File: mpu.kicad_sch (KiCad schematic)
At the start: 10 parts, among them U501 STM32MP135FAE7

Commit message: Reorganize schema
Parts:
- renumbered C502 to C401, C501 to C402, R502 to R401, R501 to R402, TP501 to TP401, TP502 to TP402, TP503 to TP403, TP504 to TP404, TP505 to TP405, U501 to U401
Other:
- added sheet MPU PMIC (mpu_pmic.kicad_sch)
- moved on the sheet: C401, C402, R401, R402, TP401, TP402, TP403, TP404, TP405, U401C, U401D, U401E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

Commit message: Add MPU boot selection
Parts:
- added R403, R404, R405: 1 kΩ, perfect_footprints:R_0402_1005Metric, symbol Device:R
- added SW401: SW_DIP_x03, symbol Switch:SW_DIP_x03
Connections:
- net GND: now also SW401.4, SW401.5, SW401.6
- net VDD: now also R403.1, R404.1, R405.1
- net RX: now reaches U401.C5 (PD8)
- net TX: now reaches U401.D2 (PD6)
- net BOOT1: now reaches U401.H2 (PI3)
- net BOOT1: now also R404.2, SW401.2
- net BOOT2: now reaches U401.J3 (PI2)
- net BOOT2: now also R403.2, SW401.3
- net BOOT0: now reaches U401.U14 (PI4)
- net BOOT0: now also R405.2, SW401.1
- no-connect marks 128 -> 123
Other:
- moved on the sheet: C401, C402, R401, R402, TP401, TP402, TP403, TP404, TP405, U401C, U401D, U401E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

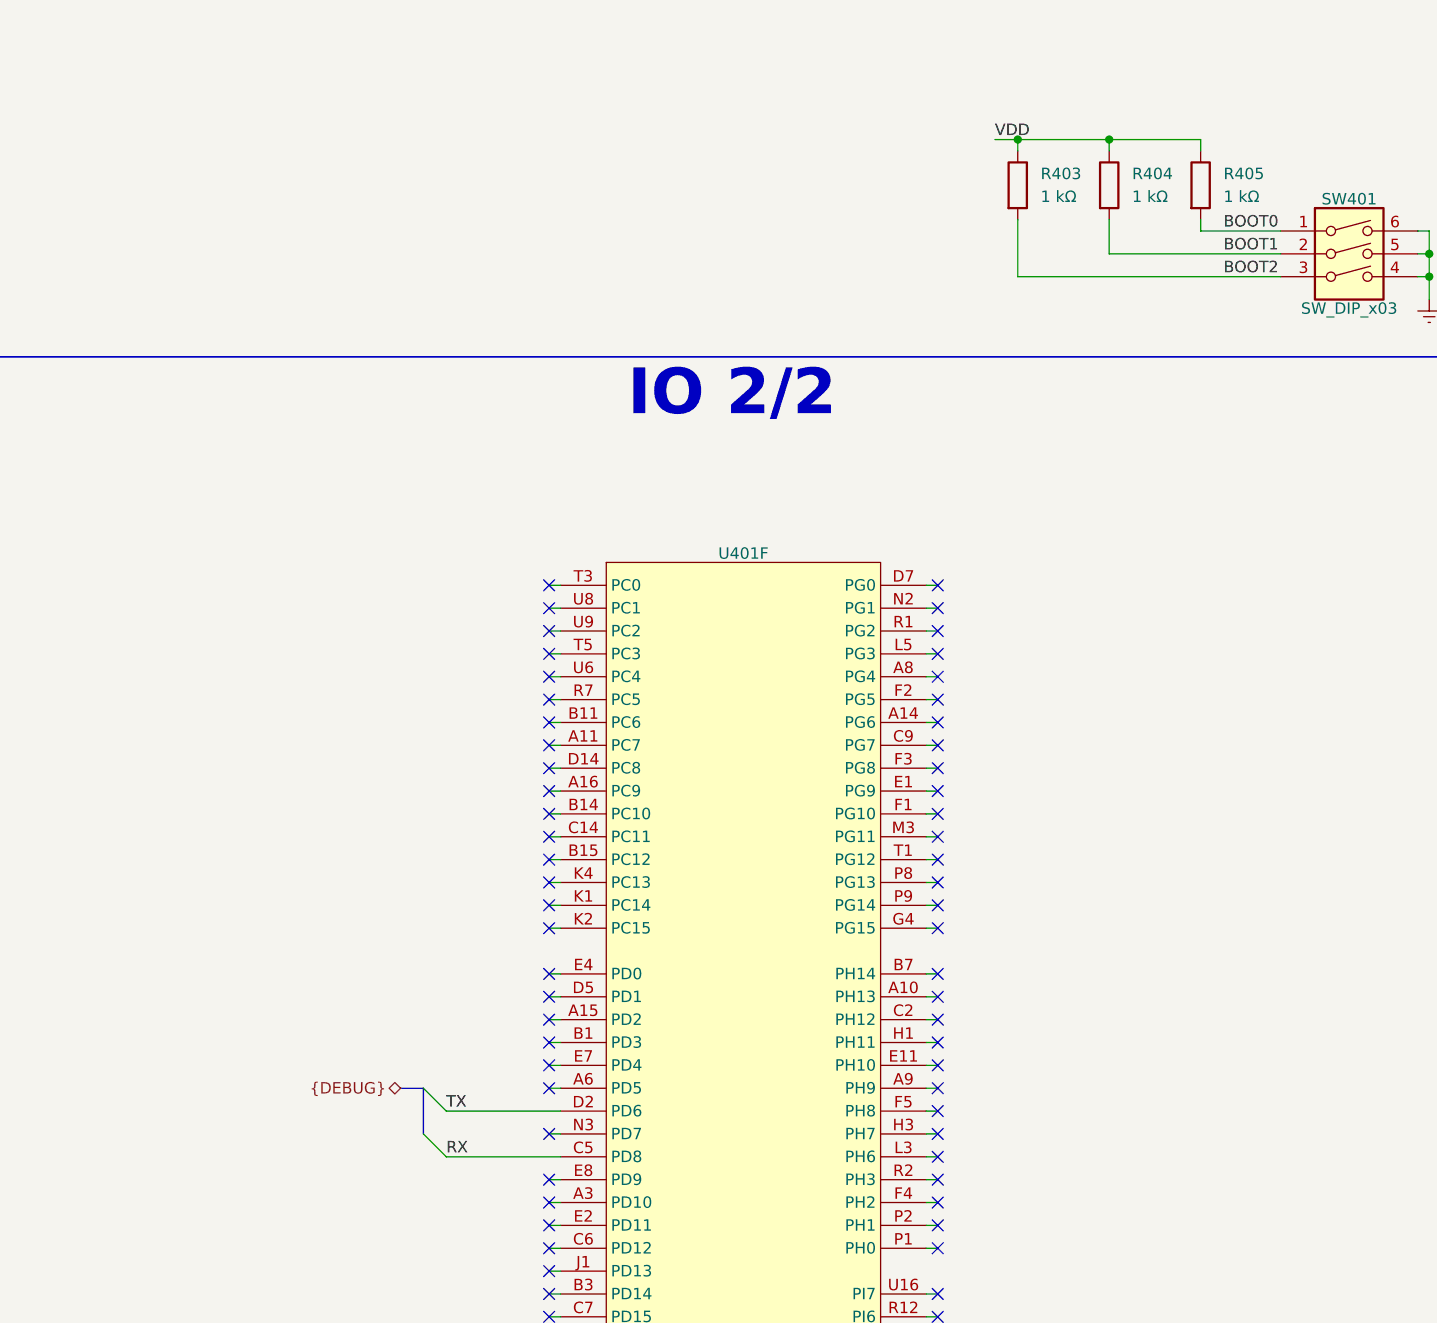
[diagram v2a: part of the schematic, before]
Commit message: Add USB-to-UART debug option
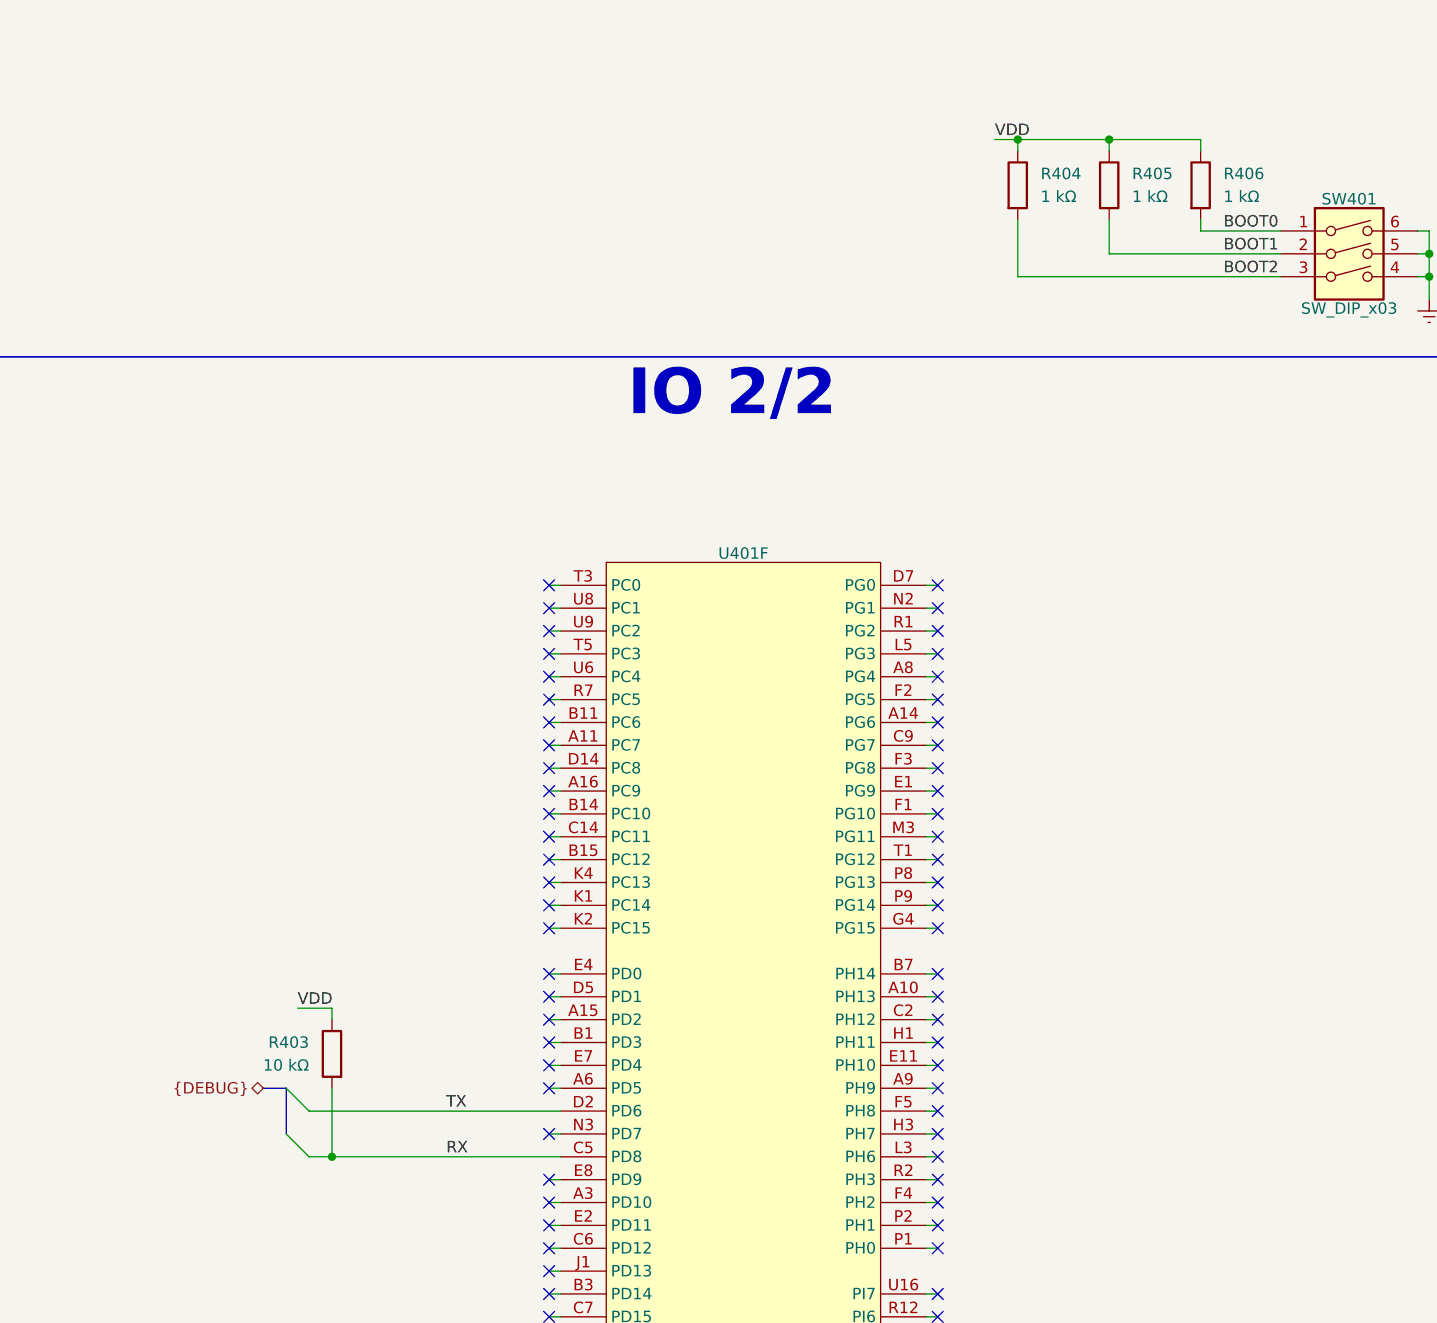
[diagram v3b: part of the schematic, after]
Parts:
- added R403: 10 kΩ, perfect_footprints:R_0402_1005Metric, symbol Device:R
- renumbered R403 to R404, R404 to R405, R405 to R406
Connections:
- net RX: now also R403.2
- net VDD: now also R403.1
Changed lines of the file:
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@@
 		(color 0 0 0 0)
 	)
+	(junction
+		(at 279.4 203.2)
+		(diameter 0)
+		(color 0 0 0 0)
+	)
 	(no_connect
 		(at 303.53 139.7)
@@
 	)
 	(bus_entry
-		(at 289.56 200.66)
+		(at 274.32 200.66)
 		(size 2.54 2.54)
 		(stroke
@@
 	)
 	(bus_entry
-		(at 289.56 195.58)
+		(at 274.32 195.58)
 		(size 2.54 2.54)
 		(stroke
@@
 		)
 	)
+	(wire
+		(pts
+			(xy 279.4 186.69) (xy 279.4 187.96)
+		)
+		(stroke
+			(width 0)
+			(type default)
+		)
+	)
 	(bus
 		(pts
@@
 	(bus
 		(pts
-			(xy 289.56 200.66) (xy 289.56 195.58)
+			(xy 274.32 200.66) (xy 274.32 195.58)
 		)
 		(stroke
@@
 	(wire
 		(pts
+			(xy 279.4 195.58) (xy 279.4 203.2)
+		)
+		(stroke
+			(width 0)
+			(type default)
+		)
+	)
+	(wire
+		(pts
 			(xy 304.8 152.4) (xy 303.53 152.4)
 		)
@@
 	(wire
 		(pts
-			(xy 304.8 203.2) (xy 292.1 203.2)
+			(xy 304.8 203.2) (xy 279.4 203.2)
 		)
 		(stroke
@@
 		)
 	)
+	(wire
+		(pts
+			(xy 279.4 203.2) (xy 276.86 203.2)
+		)
+		(stroke
+			(width 0)
+			(type default)
+		)
+	)
 	(bus
 		(pts
@@
 	(bus
 		(pts
-			(xy 287.02 195.58) (xy 289.56 195.58)
+			(xy 271.78 195.58) (xy 274.32 195.58)
 		)
 		(stroke
@@
 		)
 	)
+	(wire
+		(pts
+			(xy 275.59 186.69) (xy 279.4 186.69)
+		)
+		(stroke
+			(width 0)
+			(type default)
+		)
+	)
 	(bus
 		(pts
@@
 	(wire
 		(pts
-			(xy 304.8 198.12) (xy 292.1 198.12)
+			(xy 304.8 198.12) (xy 276.86 198.12)
 		)
 		(stroke
@@
 		)
 	)
+	(label "VDD"
+		(at 275.59 186.69 0)
+		(effects
+			(font
+				(size 1.27 1.27)
+			)
+			(justify left bottom)
+		)
+	)
 	(label "DQ14"
 		(at 100.33 190.5 180)
@@
 	(hierarchical_label "{DEBUG}"
 		(shape bidirectional)
-		(at 287.02 195.58 180)
+		(at 271.78 195.58 180)
 		(effects
 			(font
@@
 	)
 	(symbol
+		(lib_id "Device:R")
+		(at 279.4 191.77 0)
+		(mirror y)
+		(unit 1)
+		(exclude_from_sim no)
+		(in_bom yes)
+		(on_board yes)
+		(dnp no)
+		(property "Reference" "R403"
+			(at 276.86 190.4999 0)
+			(effects
+				(font
+					(size 1.27 1.27)
+				)
+				(justify left)
+			)
+		)
+		(property "Value" "10 kΩ"
+			(at 276.86 193.0399 0)
+			(effects
+				(font
+					(size 1.27 1.27)
+				)
+				(justify left)
+			)
+		)
+		(property "Footprint" "perfect_footprints:R_0402_1005Metric"
+			(at 281.178 191.77 90)
+			(effects
+				(font
+					(size 1.27 1.27)
+				)
+				(hide yes)
+			)
+		)
+		(property "Datasheet" "https://www.we-online.com/components/products/datasheet/560112110020.pdf"
+			(at 279.4 191.77 0)
+			(effects
+				(font
+					(size 1.27 1.27)
+				)
+				(hide yes)
+			)
+		)
+		(property "Description" "Resistor"
+			(at 279.4 191.77 0)
+			(effects
+				(font
+					(size 1.27 1.27)
+				)
+				(hide yes)
+			)
+		)
+		(property "DigiKey Part Number" "732-560112110020CT-ND"
+			(at 279.4 191.77 0)
+			(effects
+				(font
+					(size 1.27 1.27)
+				)
+				(hide yes)
+			)
+		)
+		(property "MPN" "560112110020"
+			(at 279.4 191.77 0)
+			(effects
+				(font
+					(size 1.27 1.27)
+				)
+				(hide yes)
+			)
+		)
+		(property "Manufacturer" "Würth Elektronik"
+			(at 279.4 191.77 0)
+			(effects
+				(font
+					(size 1.27 1.27)
+				)
+				(hide yes)
+			)
+		)
+		(property "Temperature Coefficient" ""
+			(at 279.4 191.77 0)
+			(effects
+				(font
+					(size 1.27 1.27)
+				)
+				(hide yes)
+			)
+		)
+		(pin "2"
+		)
+		(pin "1"
+		)
+		(instances
+			(project "linux-sbc"
+				(path "/fa11a02f-8043-4153-ab69-88d766503017/2d01087b-54dc-4f43-9cc7-a0ba17201776"
+					(reference "R403")
+					(unit 1)
+				)
+			)
+		)
+	)
+	(symbol
 		(lib_id "Connector:TestPoint")
 		(at 232.41 76.2 0)
@@
 		(on_board yes)
 		(dnp no)
-		(property "Reference" "R405"
+		(property "Reference" "R406"
 			(at 378.46 93.9799 0)
 			(effects
@@
 			(project "linux-sbc"
 				(path "/fa11a02f-8043-4153-ab69-88d766503017/2d01087b-54dc-4f43-9cc7-a0ba17201776"
-					(reference "R405")
+					(reference "R406")
 					(unit 1)
 				)
@@
 		(on_board yes)
 		(dnp no)
-		(property "Reference" "R403"
+		(property "Reference" "R404"
 			(at 358.14 93.9799 0)
 			(effects
@@
 			(project "linux-sbc"
 				(path "/fa11a02f-8043-4153-ab69-88d766503017/2d01087b-54dc-4f43-9cc7-a0ba17201776"
-					(reference "R403")
+					(reference "R404")
 					(unit 1)
 				)
@@
 		(on_board yes)
 		(dnp no)
-		(property "Reference" "R404"
+		(property "Reference" "R405"
 			(at 368.3 93.9799 0)
 			(effects
@@
 			(project "linux-sbc"
 				(path "/fa11a02f-8043-4153-ab69-88d766503017/2d01087b-54dc-4f43-9cc7-a0ba17201776"
-					(reference "R404")
+					(reference "R405")
 					(unit 1)
 				)

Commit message: Add a debug section
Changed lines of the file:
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@@
 	)
 	(junction
+		(at 83.82 92.71)
+		(diameter 0)
+		(color 0 0 0 0)
+	)
+	(junction
 		(at 401.32 105.41)
 		(diameter 0)
@@
 	(wire
 		(pts
+			(xy 83.82 92.71) (xy 99.06 92.71)
+		)
+		(stroke
+			(width 0)
+			(type default)
+		)
+	)
+	(wire
+		(pts
 			(xy 345.44 205.74) (xy 346.71 205.74)
 		)
@@
 	(wire
 		(pts
+			(xy 86.36 90.17) (xy 83.82 90.17)
+		)
+		(stroke
+			(width 0)
+			(type default)
+		)
+	)
+	(wire
+		(pts
+			(xy 83.82 90.17) (xy 83.82 92.71)
+		)
+		(stroke
+			(width 0)
+			(type default)
+		)
+	)
+	(wire
+		(pts
 			(xy 73.66 87.63) (xy 86.36 87.63)
 		)
@@
 	(wire
 		(pts
-			(xy 353.06 90.17) (xy 355.6 90.17)
+			(xy 354.33 90.17) (xy 355.6 90.17)
 		)
 		(stroke
@@
 	(wire
 		(pts
-			(xy 73.66 92.71) (xy 99.06 92.71)
+			(xy 73.66 92.71) (xy 83.82 92.71)
 		)
 		(stroke
@@
 	(wire
 		(pts
-			(xy 275.59 186.69) (xy 279.4 186.69)
+			(xy 278.13 186.69) (xy 279.4 186.69)
 		)
 		(stroke
@@
 		)
 	)
-	(label "VDD"
-		(at 275.59 186.69 0)
-		(effects
-			(font
-				(size 1.27 1.27)
-			)
-			(justify left bottom)
-		)
-	)
 	(label "DQ14"
 		(at 100.33 190.5 180)
@@
 		)
 	)
-	(label "VDD"
-		(at 353.06 90.17 0)
-		(effects
-			(font
-				(size 1.27 1.27)
-			)
-			(justify left bottom)
-		)
-	)
 	(label "A11"
 		(at 34.29 180.34 0)
@@
 		)
 	)
-	(label "VDD"
-		(at 214.63 86.36 180)
-		(effects
-			(font
-				(size 1.27 1.27)
-			)
-			(justify right bottom)
-		)
-	)
 	(label "A2"
 		(at 34.29 157.48 0)
@@
 		)
 	)
-	(label "VDD"
-		(at 86.36 92.71 180)
-		(effects
-			(font
-				(size 1.27 1.27)
-			)
-			(justify right bottom)
-		)
-	)
 	(label "A13"
 		(at 34.29 185.42 0)
@@
 		)
 	)
+	(hierarchical_label "VDD"
+		(shape output)
+		(at 354.33 90.17 180)
+		(effects
+			(font
+				(size 1.27 1.27)
+			)
+			(justify right)
+		)
+	)
+	(hierarchical_label "VDD"
+		(shape output)
+		(at 214.63 86.36 0)
+		(effects
+			(font
+				(size 1.27 1.27)
+			)
+			(justify left)
+		)
+	)
 	(hierarchical_label "{PMIC}"
 		(shape bidirectional)
@@
 		)
 	)
+	(hierarchical_label "VDD"
+		(shape output)
+		(at 86.36 90.17 0)
+		(effects
+			(font
+				(size 1.27 1.27)
+			)
+			(justify left)
+		)
+	)
 	(hierarchical_label "VREF_DDR"
 		(shape output)
@@
 		)
 	)
+	(hierarchical_label "VDD"
+		(shape output)
+		(at 278.13 186.69 180)
+		(effects
+			(font
+				(size 1.27 1.27)
+			)
+			(justify right)
+		)
+	)
